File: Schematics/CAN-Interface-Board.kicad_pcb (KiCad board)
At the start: 4 copper layers, 50 x 100 mm, 72 parts, among them CN1 Limit Switch Connector 1, CN2 Limit Switch Connector 2, J1 Microsemi_FlashPro-JTAG-10, J2 USB_C_Receptacle, J3 Micro_SD_Card, J4 Screw_Terminal_01x02, J5 Screw_Terminal_01x02, J6 Conn_01x05_Pin, U1 SN65HVD230, U2 LDL1117-3.3, U3 STM32F405RGT6, U5 LSM6DS3TR-C, U7 Bosch BMP388, Y1 8mhz

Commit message: final draft, in JLPCB cart
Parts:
- removed D3, D6: D_Schottky, Diode_SMD:D_SOD-123
- CN1, CN2: footprint myFootprints:JST_B2B-XH-A_LF__SN_ -> Connector_JST:JST_EH_B2B-EH-A_1x02_P2.50mm_Vertical
- J3: footprint Connector_Card:microSD_HC_Molex_104031-0811 -> Connector_Card:microSD_HC_Molex_47219-2001
- J4, J5: footprint Connector_JST:JST_XH_B2B-XH-AM_1x02_P2.50mm_Vertical -> Connector_JST:JST_EH_B2B-EH-A_1x02_P2.50mm_Vertical
- moved R8 2.21 mm to (127.9, 75.0)
- moved R9 1.66 mm to (126.5, 69.6)
- moved J3 1.33 mm to (117.8, 72.8)
- moved CN2 1.20 mm to (157.1, 103.4)
- moved J4 1.18 mm to (157.1, 86.1)
- moved R13 1.15 mm to (156.9, 107.7)
- moved J5 1.15 mm to (157.1, 94.7)
- moved CN1 1.10 mm to (157.0, 115.8)
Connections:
- CN1 pad 1: +3.3V -> /MCU/LimitSwitchCAS
- CN1 pad 2: /MCU/LimitSwitchCAS -> +3.3V
- CN2 pad 1: +3.3V -> /MCU/LimitSwitchRoll
- CN2 pad 2: /MCU/LimitSwitchRoll -> +3.3V
- J4 pad 1: Net-(D3-K) -> GND
- J4 pad 2: GND -> /MCU/PWMServo_Roll
- J5 pad 1: Net-(D6-K) -> GND
- J5 pad 2: GND -> /MCU/PWMServo_CAS
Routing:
- net /MCU/5Venable: track 9.52 -> 0.00 mm, vias 1 -> 0
- net +3.3V: track 77.9 -> 83.9 mm, vias 21 -> 23
- net Net-(D6-K): track 5.09 -> 0.00 mm
- net Net-(D3-K): track 4.81 -> 0.00 mm
- net Net-(J3-CLK): track 2.73 -> 7.39 mm
- net /MCU/CurrentCheck: track 4.20 -> 0.00 mm, vias 1 -> 0
- net Net-(J3-DAT3/CD): track 2.84 -> 6.83 mm
- net /MCU/PWMServo_Roll: track 28.8 -> 24.8 mm, vias 2 -> 1
- net /MCU/LimitSwitchRoll: track 62.0 -> 58.5 mm
- net /FlashSD/SDMISO: track 36.2 -> 39.0 mm
- net GND: track 122.4 -> 120.8 mm, vias 50 -> 55
- net /FlashSD/SDCLK: track 23.5 -> 22.7 mm
- net /MCU/PWMServo_CAS: track 36.3 -> 35.5 mm, vias 2 -> 1
- added copper zone on F.Cu, net GND
- removed copper zone on F.Cu, net (none)
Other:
- board text added: "JLCJLCJLCJLC"

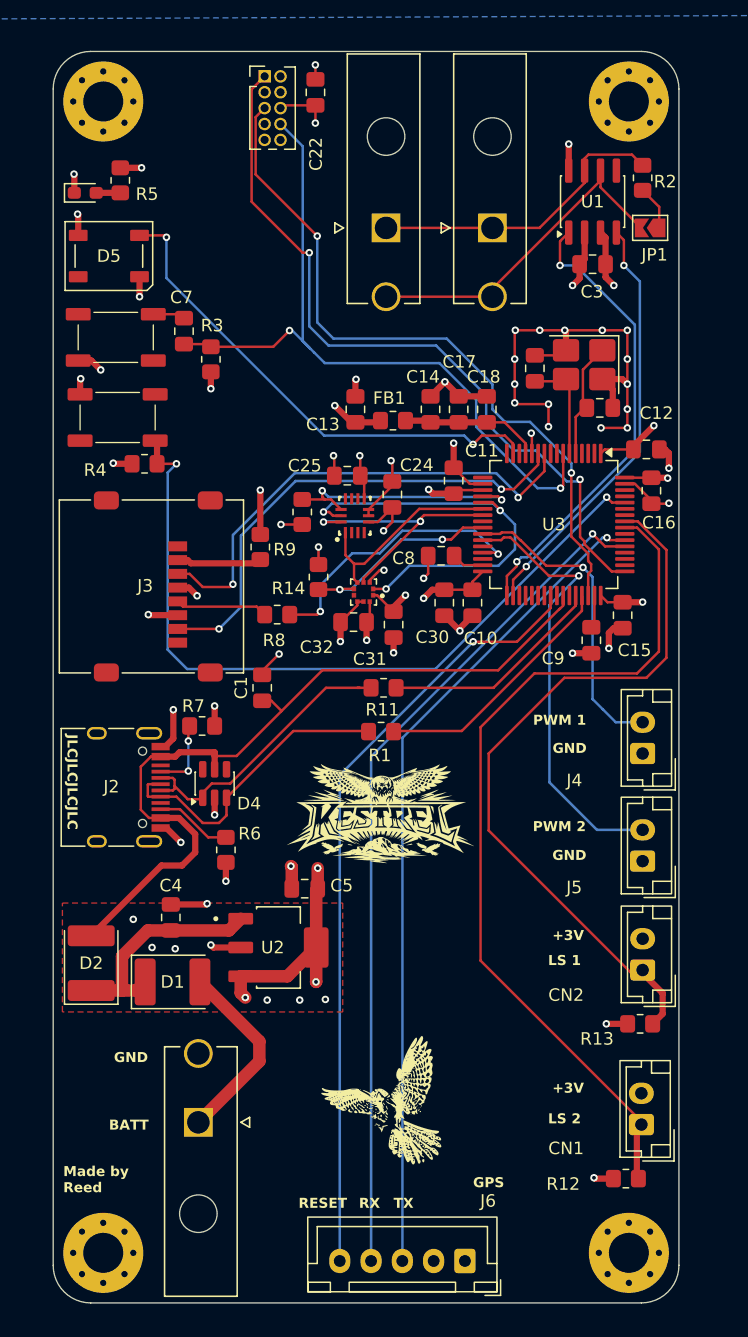
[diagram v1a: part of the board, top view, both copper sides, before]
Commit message: Added encoder connection for parafoil motor position information, in buy order ready for purchase
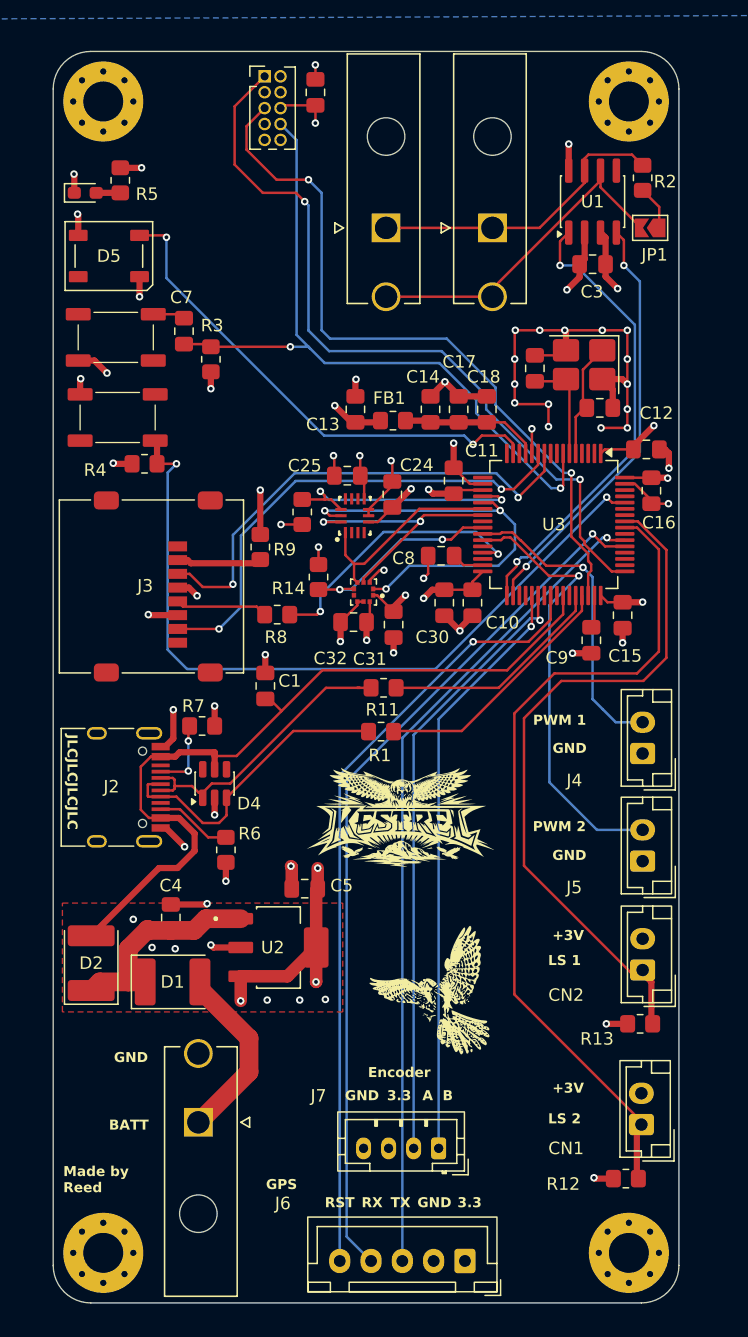
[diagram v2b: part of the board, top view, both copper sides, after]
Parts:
- added J7: Conn_01x04_Pin, Connector_JST:JST_PH_B4B-PH-K_1x04_P2.00mm_Vertical, F.Cu at (140.8, 117.7)
- moved G*** 9.61 mm to (140.2, 105.0)
- moved G*** 1.63 mm to (138.0, 92.3)
- moved C1 0.29 mm to (127.0, 80.7), turned to -90 degrees
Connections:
- C1 pad 1: /USB5V -> GND
- C1 pad 2: GND -> /USB5V
- U3 pad 37: /MCU/CurrentCheck -> /MCU/Encoder-B
- U3 pad 38: unconnected-(U3-PC7-Pad38) -> /MCU/Encoder-A
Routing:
- net /MCU/Encoder-A: track 0.00 -> 49.1 mm, vias 0 -> 1
- net /MCU/Encoder-B: track 0.00 -> 47.3 mm, vias 0 -> 1
- net /MCU/LimitSwitchCAS: track 69.8 -> 66.6 mm
- net /MCU/LimitSwitchRoll: track 58.5 -> 55.5 mm
- net /MCU/SWCLK: track 60.2 -> 62.0 mm
- net /MCU/NRST: track 59.4 -> 57.7 mm
- net /GPS1_RX: track 68.4 -> 70.0 mm
- net /MCU/SWDIO: track 56.9 -> 58.4 mm
- net Net-(D1-K): track 18.1 -> 17.3 mm
- net /USB Type C/D-: track 23.4 -> 22.7 mm
- net +BATT: track 15.7 -> 15.0 mm
- net /Barometer/Baraometer-SCK: track 34.2 -> 33.5 mm
- net /FlashSD/SDCLK: track 22.7 -> 22.2 mm
- net /RESET1: track 62.2 -> 62.7 mm
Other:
- board text added: "3.3"
- board text added: "A"
- board text added: "B"
- board text added: "Encoder"
- board text added: "RST"
- board text removed: "RESET"
